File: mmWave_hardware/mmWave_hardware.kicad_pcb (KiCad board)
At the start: 6 copper layers, 50 x 1 mm, 53 parts, among them J1 Conn_02x08_Top_Bottom, U1 IWRL6432BDBAAMFR, U2 W25Q128JVS, U3 AMS1117-3.3, U4 TPS628502QDRLRQ1, Y1 40.000

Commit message: antenna array
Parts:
- moved AE1 14.2 mm to (74.7, 56.4)
- moved AE4 1.48 mm to (83.0, 56.0)
- moved AE5 1.14 mm to (85.7, 56.4)
- moved AE2 1.14 mm to (77.5, 56.4)
- moved AE3 1.14 mm to (80.2, 56.4)

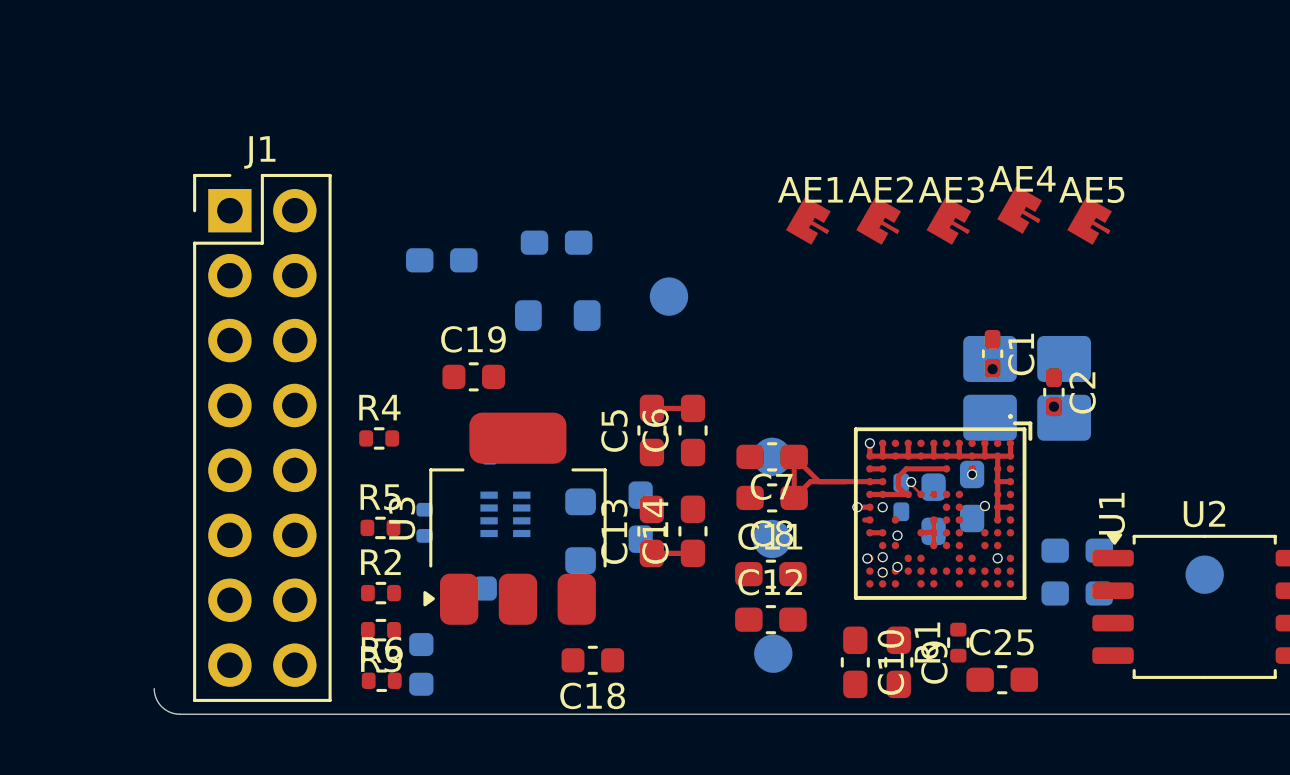
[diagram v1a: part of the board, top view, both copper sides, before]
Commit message: antennas(RX+TX)
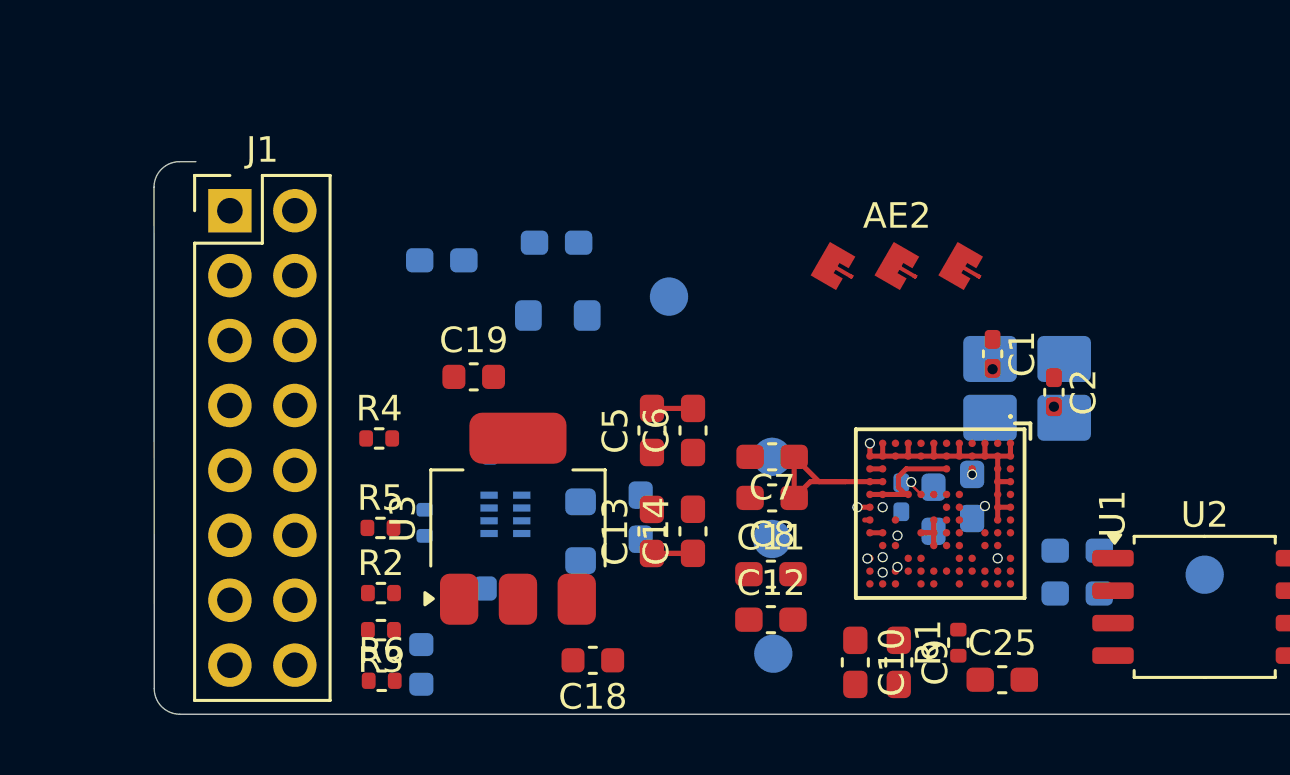
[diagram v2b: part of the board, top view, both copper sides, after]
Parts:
- removed AE1, AE3, AE4, AE5: Antenna, antennas:60GHz_microstrip_inset_patch
- AE2: footprint antennas:60GHz_microstrip_inset_patch -> antennas:RX_60GHz_microstrip_inset_patch
- moved AE2 1.18 mm to (78.1, 57.5)
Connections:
- AE2 pad 1: Net-(AE2-A) -> Net-(U1-RX1)
- U1 pad A3: Net-(AE2-A) -> Net-(U1-TX1)
- U1 pad F1: Net-(AE3-A) -> Net-(U1-RX3)
- U1 pad H1: Net-(AE4-A) -> Net-(U1-RX2)
- U1 pad K1: Net-(AE5-A) -> Net-(U1-RX1)
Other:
- board size 50 x 1 mm -> 50 x 21.6 mm

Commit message: Layout Complete
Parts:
- removed the C18 at (1.50, 0.76)
- removed the C18 at (66.2, 72.9)
- removed the C19 at (61.5, 61.8)
- removed the C19 at (1.50, 3.27)
- added AE1: Antenna, antennas:TX_60GHz_microstrip_inset_patch, F.Cu at (86.0, 56.7)
- added C18: 10u, Capacitor_SMD:C_0603_1608Metric, F.Cu at (64.7, 72.9)
- added C19: 10u, Capacitor_SMD:C_0603_1608Metric, F.Cu at (61.3, 61.6)
- Y1: footprint Crystal:Crystal_SMD_3225-4Pin_3.2x2.5mm_HandSoldering -> Crystal:Crystal_SMD_3225-4Pin_3.2x2.5mm
- moved L2 9.78 mm to (70.2, 67.6), turned to -90 degrees
- moved C2 1.53 mm to (83.5, 61.1)
- moved AE2 0.80 mm to (77.9, 56.7)
- moved C1 0.38 mm to (82.1, 61.1)
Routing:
- net /CLKM: track 0.00 -> 2.91 mm
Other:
- outline, holes or cut-outs redrawn

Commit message: pcb
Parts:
- R1: moved to B.Cu
- moved C3 10.4 mm to (75.3, 66.9), turned to -90 degrees
- moved TP1 7.74 mm to (76.1, 72.1)
- moved TP5 6.02 mm to (73.2, 63.1)
- moved TP4 4.43 mm to (73.2, 68.2)
- moved TP2 3.96 mm to (73.2, 72.1)
- moved TP3 2.19 mm to (89.3, 67.5)
- moved C4 1.00 mm to (85.2, 67.6)
- moved L1 0.54 mm to (65.7, 67.3)
- moved R1 0.42 mm to (80.6, 72.6)
- moved C18 0.28 mm to (64.7, 73.2)
- moved C17 0.24 mm to (81.0, 66.2)
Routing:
- net SPI0_CS0_N: track 0.00 -> 44.3 mm, vias 0 -> 1
- net SPI0_MISO: track 0.00 -> 37.7 mm, vias 0 -> 1
- net SPI0_CLK: track 0.00 -> 32.3 mm, vias 0 -> 1
- net SPI0_MOSI: track 0.00 -> 32.1 mm, vias 0 -> 1
- net RS232_TX: track 0.00 -> 30.4 mm, vias 0 -> 2
- net UART_TX: track 0.00 -> 26.5 mm, vias 0 -> 1
- net 3v3: track 0.00 -> 21.0 mm, vias 0 -> 3
- net VIN: track 0.00 -> 17.9 mm, vias 0 -> 3
- net /QSPI_0: track 0.00 -> 13.1 mm, vias 0 -> 2
- net /QSPI_3: track 0.00 -> 12.9 mm
- net /QSPI_CLK: track 0.00 -> 12.5 mm
- net GND: track 12.6 -> 23.6 mm, vias 2 -> 4
- net Net-(C5-Pad2): track 2.11 -> 10.0 mm
- net NRST_MAIN: track 0.00 -> 6.13 mm
- net Net-(U1-GPADC2): track 0.00 -> 5.87 mm
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
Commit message: pcb
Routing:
- net UART_RX: track 2.01 -> 40.4 mm
- net SPI0_CLK: track 32.3 -> 46.3 mm
- net SPI0_MOSI: track 32.1 -> 44.5 mm
- net UART_TX: track 26.5 -> 36.6 mm
- net SPI0_MISO: track 37.7 -> 45.4 mm
- net SPI0_CS0_N: track 44.3 -> 45.2 mm

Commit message: PCB Complete
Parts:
- Y1: footprint Crystal:Crystal_SMD_3225-4Pin_3.2x2.5mm -> Crystal:Crystal_SMD_3225-4Pin_3.2x2.5mm_HandSoldering
- moved C3 8.80 mm to (83.9, 69.0)
- moved C24 8.45 mm to (65.6, 63.8), turned to 90 degrees
- moved C23 6.27 mm to (69.3, 60.9)
- moved C9 1.74 mm to (76.5, 73.6), turned to 180 degrees
- moved C4 1.52 mm to (85.7, 69.0), turned to -90 degrees
- moved AE1 1.04 mm to (84.9, 56.7)
- moved C10 1.03 mm to (76.5, 71.9), turned to 180 degrees
- moved AE2 1.00 mm to (76.9, 56.7)
- moved U2 0.90 mm to (91.0, 70.8)
- moved C20 0.74 mm to (60.2, 73.1), turned to 0 degrees
- moved L1 0.34 mm to (65.6, 67.6)
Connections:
- J1 pad 2: TCK -> GPIO_2
- J1 pad 3: TMS -> unconnected-(J1-Pin_3-Pad3)
- J1 pad 4: TDI -> GPIO_5
- J1 pad 5: TDO -> unconnected-(J1-Pin_5-Pad5)
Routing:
- net GND: track 23.6 -> 84.8 mm, vias 4 -> 20
- net RS232_RX: track 5.25 -> 51.0 mm
- net 3v3: track 21.0 -> 66.2 mm, vias 3 -> 4
- net GPIO_5: track 0.68 -> 41.8 mm
- net GPIO_2: track 0.14 -> 39.0 mm
- net UART_RTS: track 0.87 -> 36.3 mm
- net NRST_MAIN: track 6.13 -> 35.4 mm
- net 1v8: track 12.7 -> 41.0 mm, vias 3 -> 5
- net RS232_TX: track 30.4 -> 47.4 mm
- net Net-(U4-FB): track 0.00 -> 8.63 mm
- net /QSPI_1: track 5.50 -> 13.0 mm
- net Net-(U1-OSC_CLK_OUT): track 0.00 -> 6.96 mm
- net VIN: track 17.9 -> 23.0 mm
- net 1v2: track 6.57 -> 11.0 mm
- net SPI0_CLK: track 46.3 -> 50.5 mm
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- added copper zone on B.Cu, net GND
- added copper zone on F.Cu, net GND
- added copper zone on In1.Cu, net GND
- added copper zone on In2.Cu, net GND
- added copper zone on In3.Cu, net GND
- added copper zone on In4.Cu, net GND
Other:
- board size 50 x 21.6 mm -> 49 x 21.6 mm

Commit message: pcb
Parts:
- moved TP3 1.84 mm to (90.2, 69.1)
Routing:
- net Net-(U1-OSC_CLK_OUT): track 6.96 -> 8.63 mm, vias 1 -> 2
- net GND: track 84.8 -> 83.6 mm, vias 20 -> 520
- net Net-(U1-RX1): track 0.00 -> 0.82 mm
- net Net-(U1-TX2): track 0.00 -> 0.82 mm
- net Net-(U1-TX1): track 0.00 -> 0.82 mm
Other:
- board text added: "Keyaan Was here Het was not here"
- board text added: "THE"

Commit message: pcb
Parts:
- Y1: footprint Crystal:Crystal_SMD_3225-4Pin_3.2x2.5mm_HandSoldering -> Crystal:Crystal_SMD_3225-4Pin_3.2x2.5mm
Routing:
- net GND: track 83.6 -> 75.7 mm, vias 520 -> 759
